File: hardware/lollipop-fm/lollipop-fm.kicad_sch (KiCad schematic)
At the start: 0 parts

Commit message: - imported old schematic
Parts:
- added C? (x4): 1u, Capacitor_SMD:C_0603_1608Metric, symbol Device:C
- added C? (x7): 100n, Capacitor_SMD:C_0603_1608Metric, symbol Device:C
- added C?: 4u7, Capacitor_SMD:C_0603_1608Metric, symbol Device:C
- added C? (x3): 10u, Capacitor_SMD:C_0603_1608Metric, symbol Device:C
- added C? (x2): 10p, Capacitor_SMD:C_0603_1608Metric, symbol Device:C
- added D? (x2): LED, LED_THT:LED_D3.0mm, symbol Device:LED
- added D?: ESD9B3.3ST5G, Diode_SMD:D_SOD-923, symbol Diode:ESD9B3.3ST5G
- added J?: battery pads, Connector_PinHeader_2.54mm:PinHeader_2x01_P2.54mm_Vertical, symbol Connector_Generic:Conn_01x02
- added J?: USART, Connector_PinHeader_2.54mm:PinHeader_1x03_P2.54mm_Vertical, symbol Connector_Generic:Conn_01x03
- added J?: SWD, Connector_PinHeader_2.54mm:PinHeader_1x04_P2.54mm_Vertical, symbol Connector_Generic:Conn_01x04
- added L?: 2400 uH, Connector_PinHeader_2.54mm:PinHeader_2x01_P2.54mm_Vertical, symbol Device:L
- added L?: 4.7uH, Inductor_SMD:L_0805_2012Metric, symbol Device:L
- added LS?: AI-1223-TWT-3V-2-R, Buzzer_Beeper:Buzzer_12x9.5RM7.6, symbol Device:Speaker
- added Q?: SSM3J338R, Package_TO_SOT_SMD:SOT-23, symbol custom_lib:SSM3J338R
- added Q? (x2): BC817, Package_TO_SOT_SMD:SOT-23, symbol Transistor_BJT:BC817
- added R? (x2): 1k, Resistor_SMD:R_0603_1608Metric, symbol Device:R
- added R? (x3): 470, Resistor_SMD:R_0603_1608Metric, symbol Device:R
- added R?: 1k5, Resistor_SMD:R_0603_1608Metric, symbol Device:R
- added R? (x11): 100k, Resistor_SMD:R_0603_1608Metric, symbol Device:R
- added R? (x4): 100, Resistor_SMD:R_0603_1608Metric, symbol Device:R
- added R?: 150, Resistor_SMD:R_0603_1608Metric, symbol Device:R
- added R?: 51, Resistor_SMD:R_0603_1608Metric, symbol Device:R
- added R?: 33k, Resistor_SMD:R_0603_1608Metric, symbol Device:R
- added R?: 11k, Resistor_SMD:R_0603_1608Metric, symbol Device:R
- added SW?: MJTP1230F, Button_Switch_THT:SW_PUSH_6mm, symbol Switch:SW_Push
- added U?: STM32C011F6Ux, Package_DFN_QFN:ST_UFQFPN-20_3x3mm_P0.5mm, symbol MCU_ST_STM32C0:STM32C011F6Ux
- added U? (x2): TLV9101IDCKR, Package_TO_SOT_SMD:SOT-23-5, symbol custom_lib:TLV9101IDCKR
- added U?: TPS61221DCK, Package_TO_SOT_SMD:Texas_R-PDSO-G6, symbol Regulator_Switching:TPS61221DCK
- added Y?: ECS-80-12-33-JGN-TR, Crystal:Crystal_SMD_3225-4Pin_3.2x2.5mm, symbol Device:Crystal
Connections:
- new net: C?.1, U?.1 (PC15), Y?.3
- new net: C?.1, U?.20 (PC14), Y?.1
- new net: C?.1, R?.2, U?.4 (PF2)
- new net: R?.1, R?.1, R?.1
- new net: Q?.3, R?.2
- new net: C?.1, C?.2, L?.2
- new net: C?.2, Q?.1 (B), R?.1, R?.2
- new net: Q?.1 (B), R?.2, R?.2
- new net: D?.1 (K), R?.2 (x2)
- new net: C?.1, C?.2, Q?.3 (C), R?.2
- new net: J?.2 (Pin_2), R?.1, R?.1
- new net: C?.1, C?.1, L?.1
- new net: C?.1, Q?.2 (E), R?.1
- new net: LS?.2, Q?.3 (C)
- new net: D?.2 (A2), R?.1, SW?.1
- new net: LS?.1, R?.1
- new net: R?.1, R?.1, U?.4 (-)
- new net: L?.2, U?.5 (L)
- new net: J?.1 (Pin_1), R?.1, R?.1
- new net: R?.1, U?.4 (-)
- new net: C?.2, R?.1, U?.3 (+)
- new net +3.3V: C?.1, C?.1, C?.1, C?.1, C?.2, C?.2, D?.2 (A), D?.2 (A), J?.1 (Pin_1), Q?.2, R?.1, R?.2, R?.2, R?.2, R?.2, R?.2, R?.2, U?.2 (FB), U?.2 (VDD), U?.4 (VOUT), U?.5 (V+), U?.5 (V+)
- new net +BATT: C?.1, J?.2 (Pin_2), L?.1, R?.1, U?.1 (VIN), U?.3 (+), U?.6 (EN)
- new net GND: C?.1, C?.1, C?.1, C?.1, C?.2, C?.2, C?.2, C?.2, C?.2, C?.2, C?.2, C?.2, C?.2, C?.2, D?.1 (A1), J?.1 (Pin_1), J?.3 (Pin_3), J?.4 (Pin_4), Q?.2 (E), R?.1, R?.1, R?.2, R?.2, R?.2, R?.2, R?.2, SW?.2, U?.12 (PA7), U?.2 (V-), U?.2 (V-), U?.3 (GND), U?.3 (VSS), U?.5 (PA0), U?.7 (PA2), U?.9 (PA4)
- new net RX: R?.2, U?.15 (PA10/PA12)
- new net SWCLK: J?.2 (Pin_2), R?.1, U?.17 (PA14)
- new net SWDIO: J?.3 (Pin_3), R?.2, U?.16 (PA13)
- new net TX: R?.2, U?.14 (PA9/PA11)
- new net bat_lvl: R?.2, U?.1, U?.13 (PA8)
- new net control: C?.2, R?.1, R?.2, U?.6 (PA1)
- new net led_green: R?.1, U?.10 (PA5)
- new net led_yellow: R?.1, U?.11 (PA6)
- new net osc_en: Q?.1, R?.1, U?.18 (PB6)
- new net osc_out: R?.2, U?.1, U?.8 (PA3)
- new net sound: R?.1, U?.19 (PB7)
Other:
- note added: "F = ~20 kHZ"

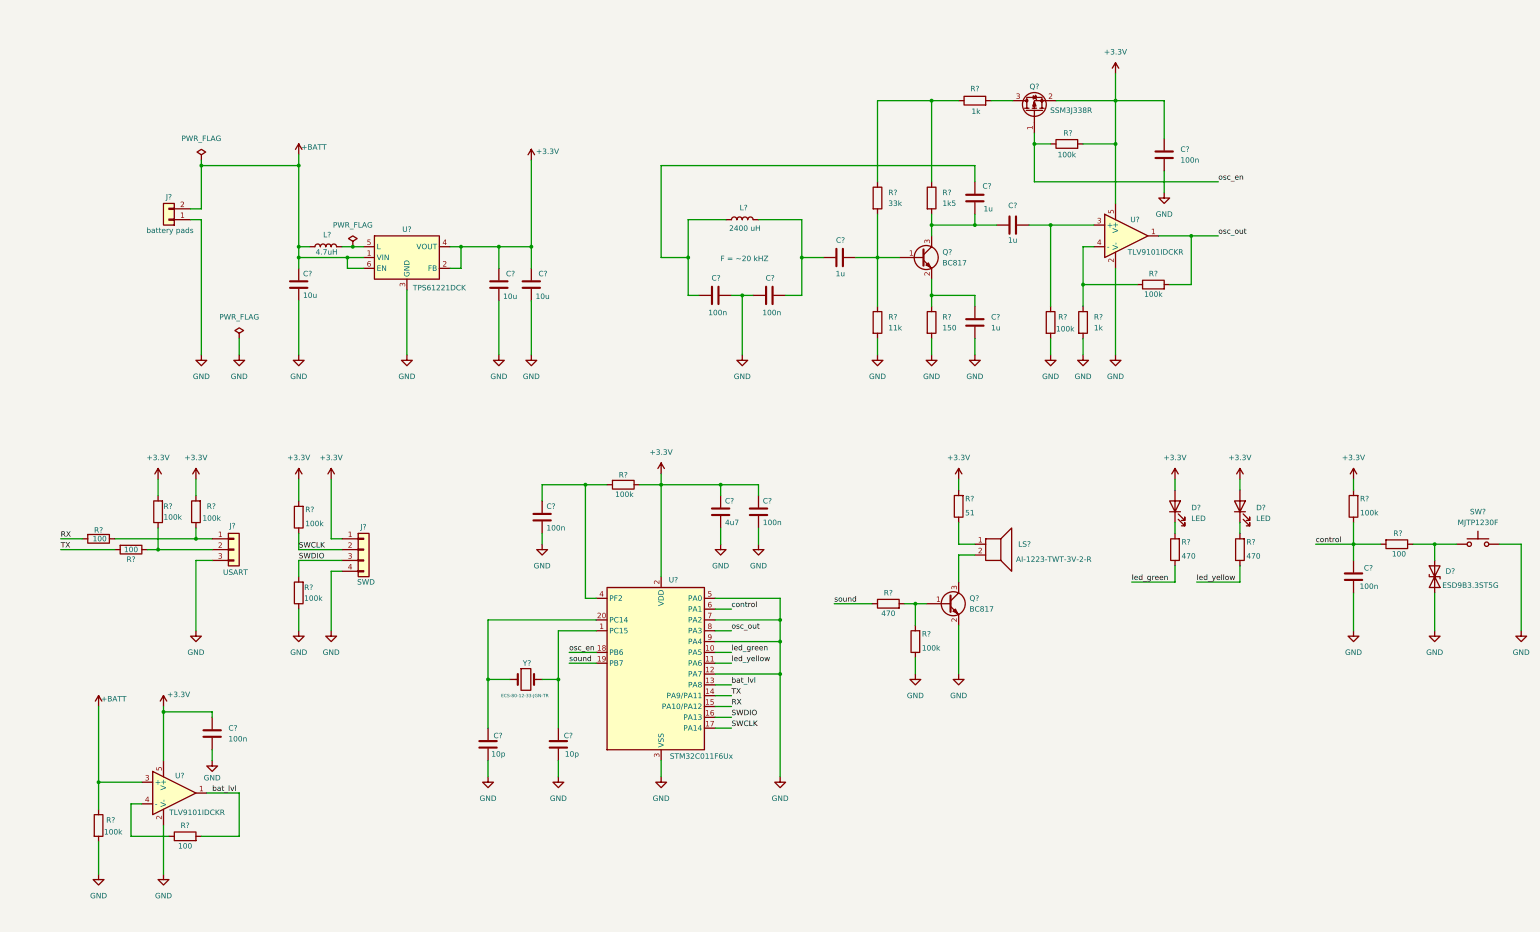
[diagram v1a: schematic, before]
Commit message: - schematic updated with latest changes
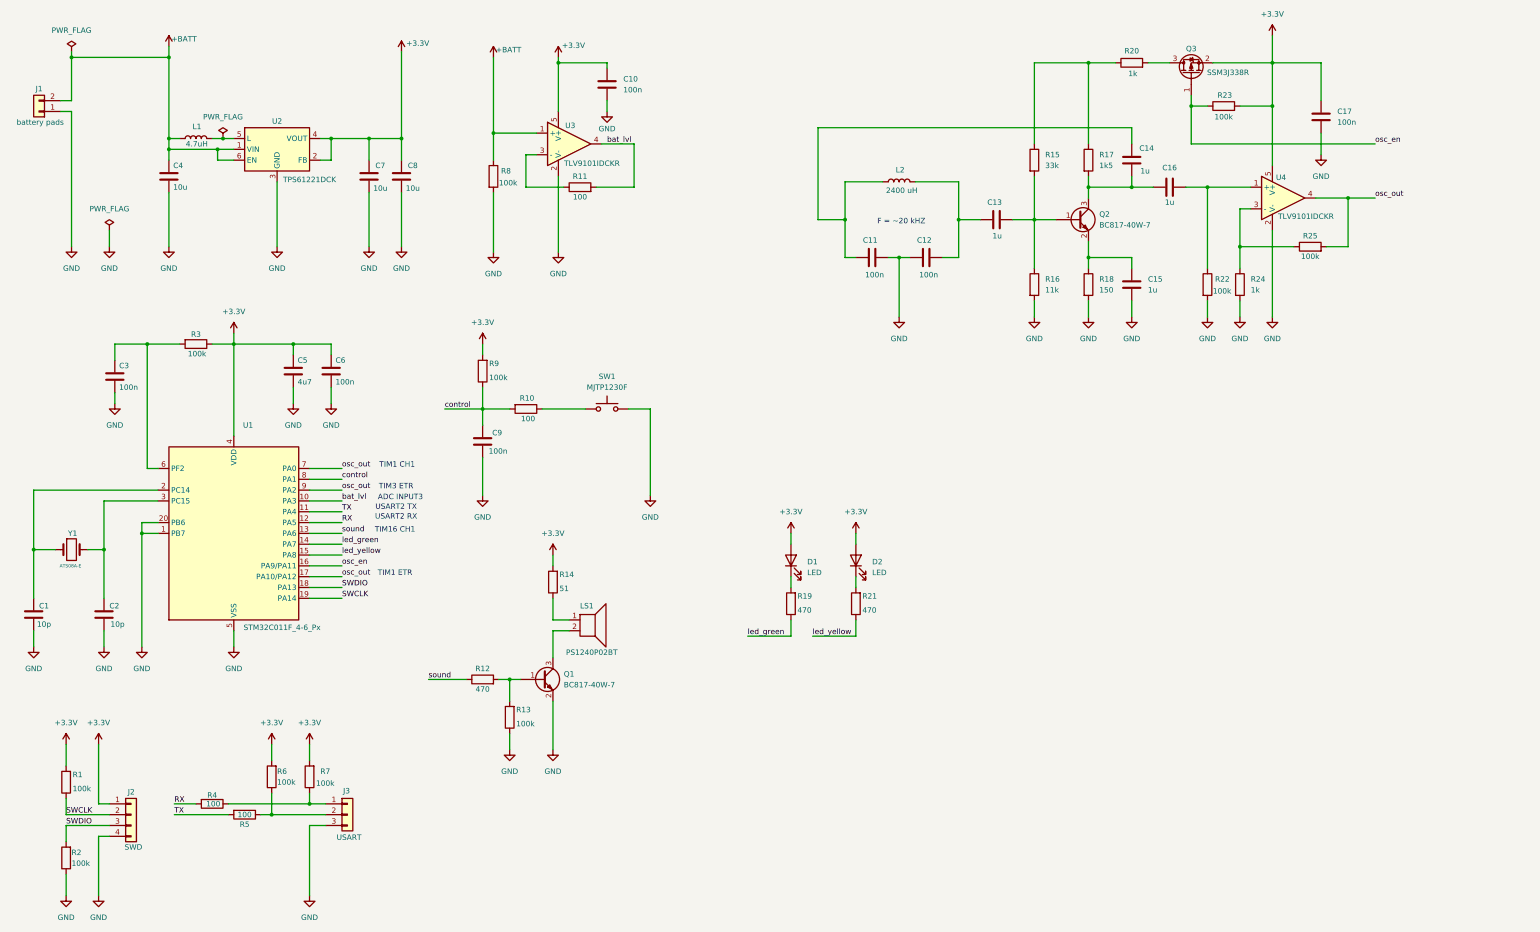
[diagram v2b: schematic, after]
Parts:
- removed D?: ESD9B3.3ST5G, Diode_SMD:D_SOD-923, symbol Diode:ESD9B3.3ST5G
- removed Q?: BC817, Package_TO_SOT_SMD:SOT-23, symbol Transistor_BJT:BC817
- removed U?: STM32C011F6Ux, Package_DFN_QFN:ST_UFQFPN-20_3x3mm_P0.5mm, symbol MCU_ST_STM32C0:STM32C011F6Ux
- removed U? (x2): TLV9101IDCKR, Package_TO_SOT_SMD:SOT-23-5, symbol custom_lib:TLV9101IDCKR
- added Q1: BC817-40W-7, Package_TO_SOT_SMD:SOT-323_SC-70_Handsoldering, symbol Transistor_BJT:BC817
- added U1: STM32C011F_4-6_Px, Package_SO:TSSOP-20_4.4x6.5mm_P0.65mm, symbol MCU_ST_STM32C0:STM32C011F_4-6_Px
- added U3, U4: TLV9101IDCKR, Package_TO_SOT_SMD:SOT-353_SC-70-5_Handsoldering, symbol custom_lib:TLV9101IDCKR
- J2: renamed from J?; footprint Connector_PinHeader_2.54mm:PinHeader_1x04_P2.54mm_Vertical -> local:pad-4-pin-2,54
- J3: renamed from J?; footprint Connector_PinHeader_2.54mm:PinHeader_1x03_P2.54mm_Vertical -> local:pad-3-pin-2,54
- LS1: renamed from LS?; value AI-1223-TWT-3V-2-R -> PS1240P02BT
- Q2: renamed from Q?; value BC817 -> BC817-40W-7; footprint Package_TO_SOT_SMD:SOT-23 -> Package_TO_SOT_SMD:SOT-323_SC-70_Handsoldering
- Y1: renamed from Y?; value ECS-80-12-33-JGN-TR -> ATS08A-E; footprint Crystal:Crystal_SMD_3225-4Pin_3.2x2.5mm -> Crystal:Crystal_HC49-4H_Vertical
- gave numbers to parts that had none: 50
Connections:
- net +3.3V: now also U1.4 (VDD), U3.5 (V+), U4.5 (V+)
- net +BATT: now also U3.1 (+)
- net GND: now also Q1.2 (E), U1.1 (PB7), U1.20 (PB6), U1.5 (VSS), U3.2 (V-), U4.2 (V-)
- net RX: now also U1.12 (PA5)
- net SWCLK: now also U1.19 (PA14)
- net SWDIO: now also U1.18 (PA13)
- net TX: now also U1.11 (PA4)
- net bat_lvl: now also U1.10 (PA3), U3.4
- net control: now also U1.8 (PA1)
- net led_green: now also U1.14 (PA7)
- net led_yellow: now also U1.15 (PA8)
- net osc_en: now also U1.16 (PA9/PA11)
- net osc_out: now also U1.17 (PA10/PA12), U1.7 (PA0), U1.9 (PA2), U4.4
- net sound: now also U1.13 (PA6)
- net at C2.1: now also Y1.2, U1.3 (PC15); no longer Y1.3
- net at C1.1, Y1.1: now also U1.2 (PC14)
- net at C3.1, R3.2: now also U1.6 (PF2)
- net at R12.2, R13.2: now also Q1.1 (B)
- net at LS1.2: now also Q1.3 (C)
- net at R24.1, R25.1: now also U4.3 (-)
- net at R11.1: now also U3.3 (-)
- net at C16.2, R22.1: now also U4.1 (+)
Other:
- note added: "ADC INPUT3"
- note added: "TIM1 CH1"
- note added: "TIM1 ETR"
- note added: "TIM16 CH1"
- note added: "TIM3 ETR"
- note added: "USART2 RX"
- note added: "USART2 TX"
- moved on the sheet: C1, C10, C11, C12, C13, C14, C15, C16, C17, C2, C3, C4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

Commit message: - new routing added
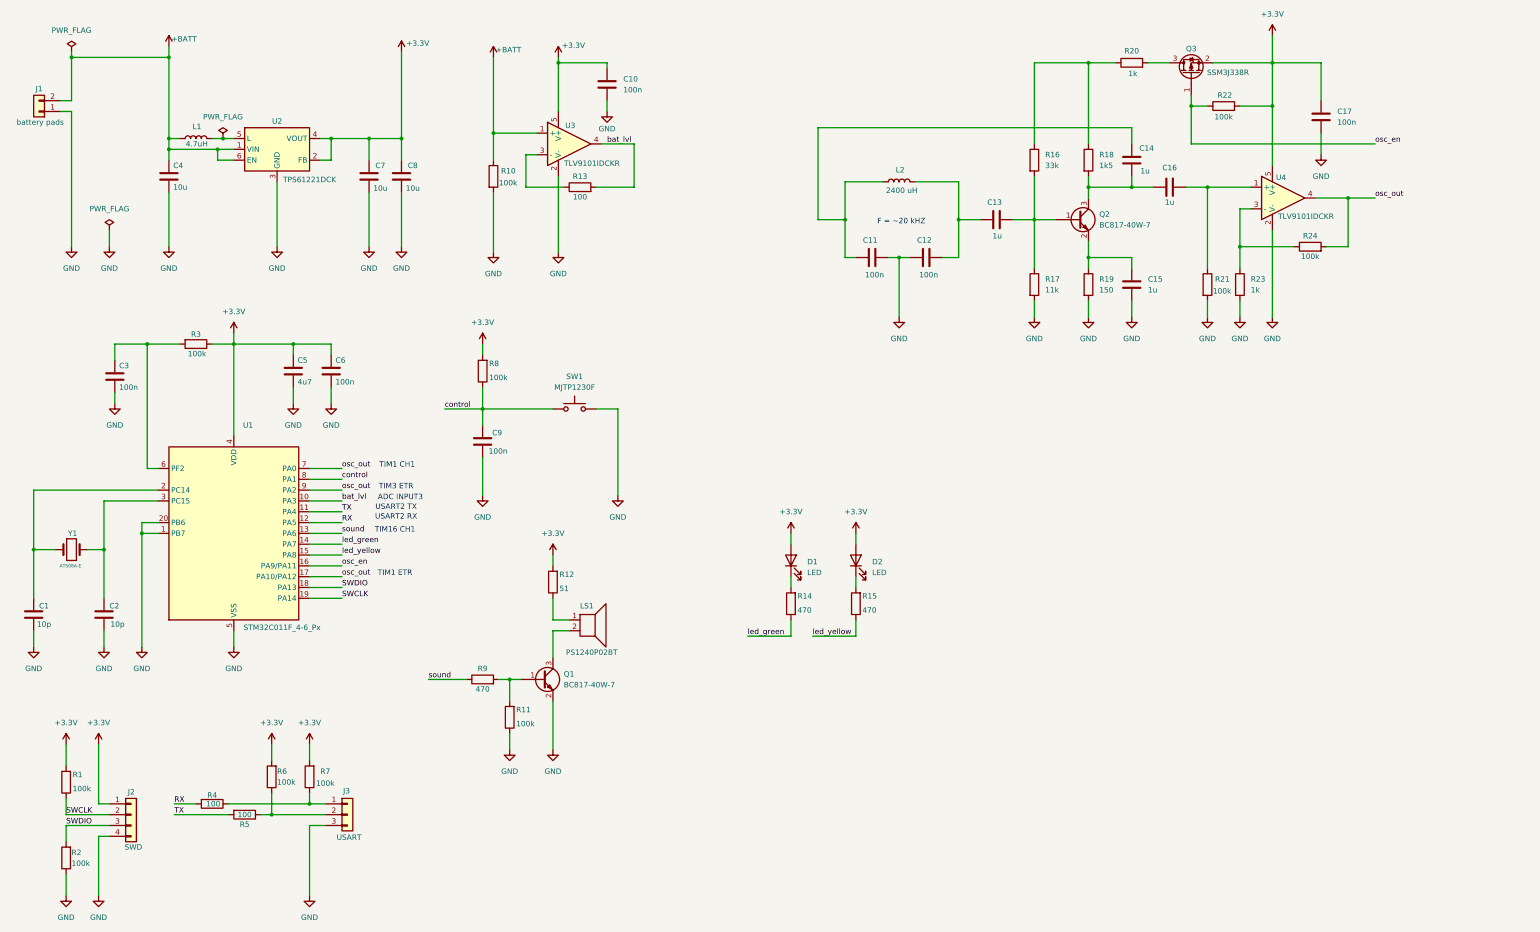
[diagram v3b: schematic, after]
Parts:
- removed R10: 100, Resistor_SMD:R_0603_1608Metric, symbol Device:R
- renumbered R8 to R10, R13 to R11, R14 to R12, R11 to R13, R19 to R14, R21 to R15, R15 to R16, R16 to R17, R17 to R18, R18 to R19, R22 to R21, R23 to R22, R24 to R23, R25 to R24, R9 to R8, R12 to R9
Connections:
- net control: now also SW1.1
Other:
- moved on the sheet: SW1

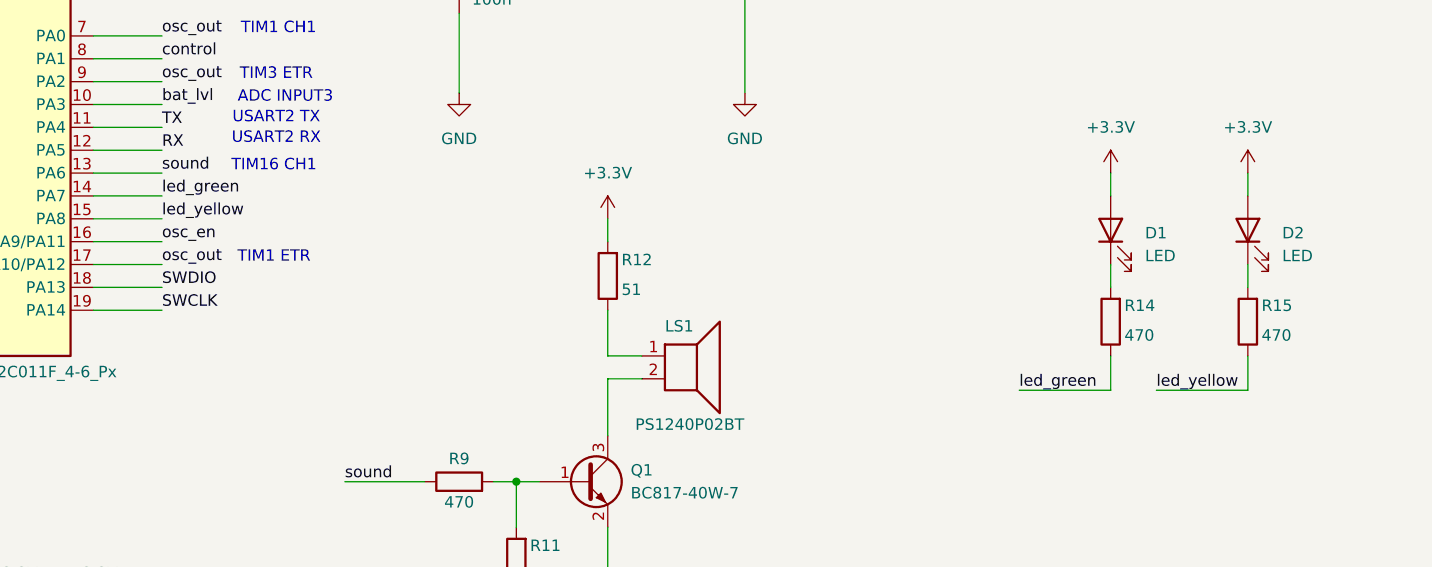
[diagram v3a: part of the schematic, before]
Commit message: - led control logic updated, schematic naming updated
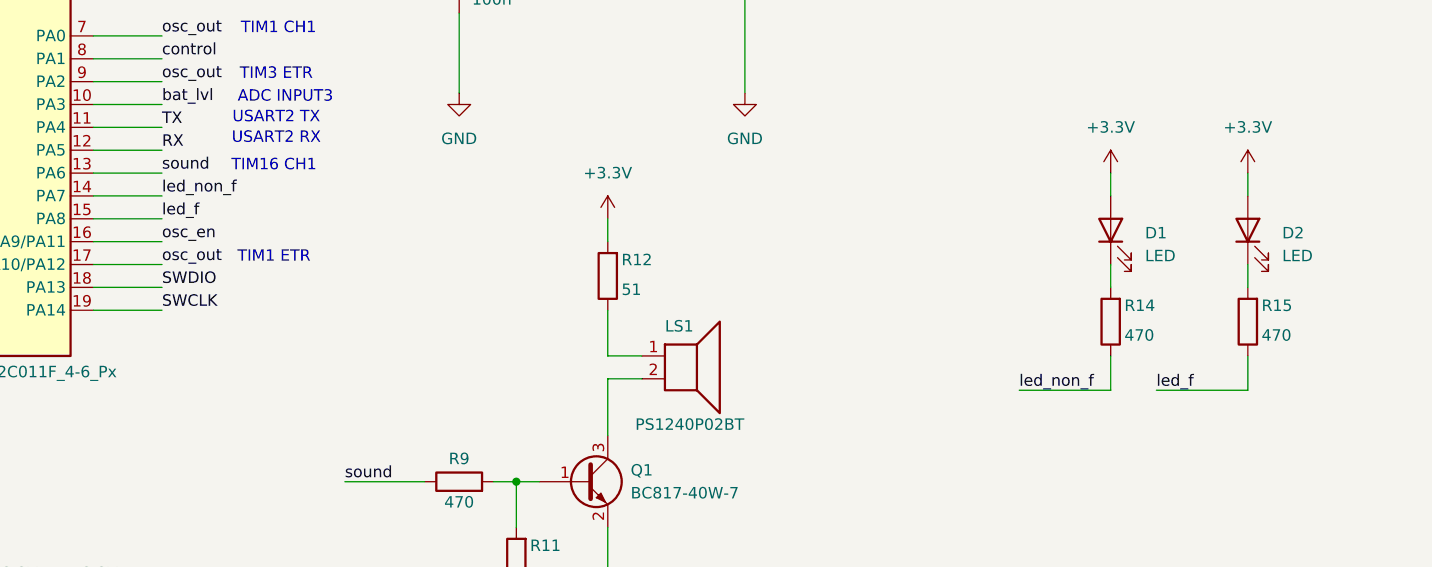
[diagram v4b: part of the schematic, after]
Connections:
- net led_green renamed led_non_f
- net led_yellow renamed led_f
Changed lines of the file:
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@@
 		)
 	)
-	(label "led_yellow"
+	(label "led_f"
 		(at 212.09 168.91 0)
 		(effects
@@
 		)
 	)
-	(label "led_green"
+	(label "led_non_f"
 		(at 196.85 168.91 0)
 		(effects
@@
 		)
 	)
-	(label "led_green"
-		(at 101.6 147.32 0)
-		(effects
-			(font
-				(size 1.27 1.27)
-			)
-			(justify left bottom)
-		)
-	)
 	(label "bat_lvl"
 		(at 101.6 137.16 0)
@@
 		)
 	)
-	(label "led_yellow"
-		(at 101.6 149.86 0)
+	(label "led_non_f"
+		(at 101.6 147.32 0)
 		(effects
 			(font
@@
 		(effects
 			(font
+				(size 1.27 1.27)
+			)
+			(justify left bottom)
+		)
+	)
+	(label "led_f"
+		(at 101.6 149.86 0)
+		(effects
+			(font
